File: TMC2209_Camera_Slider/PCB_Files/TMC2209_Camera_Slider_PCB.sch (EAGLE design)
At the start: 16 parts, among them J1 1X2-3.5MM

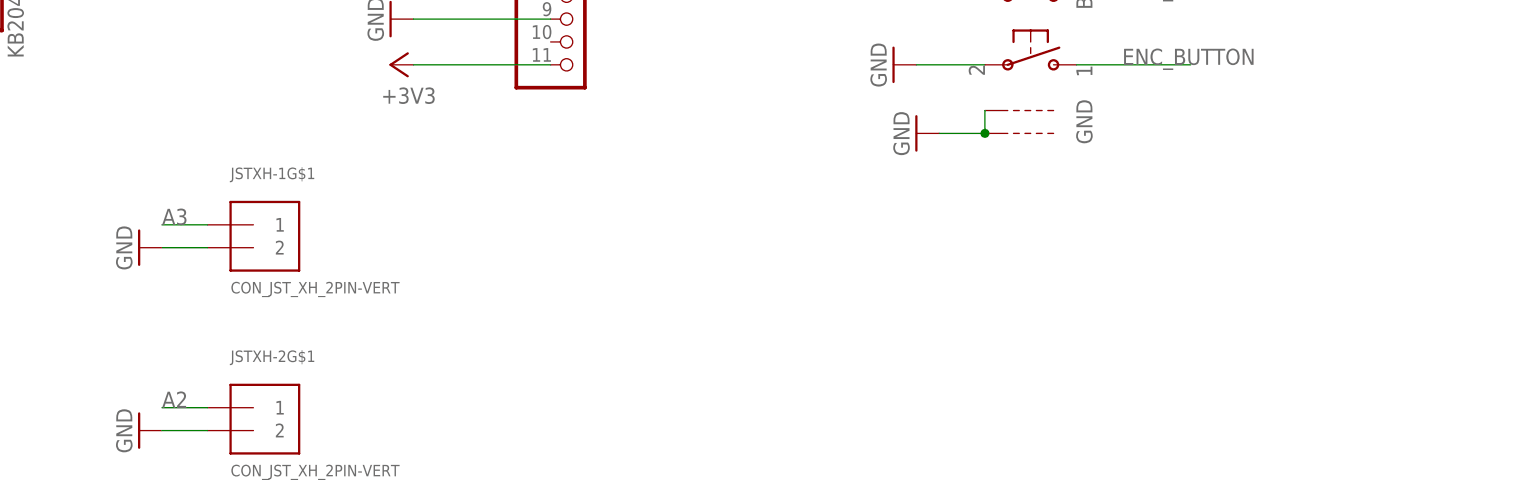
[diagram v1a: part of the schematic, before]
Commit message: switch jst xh connectors
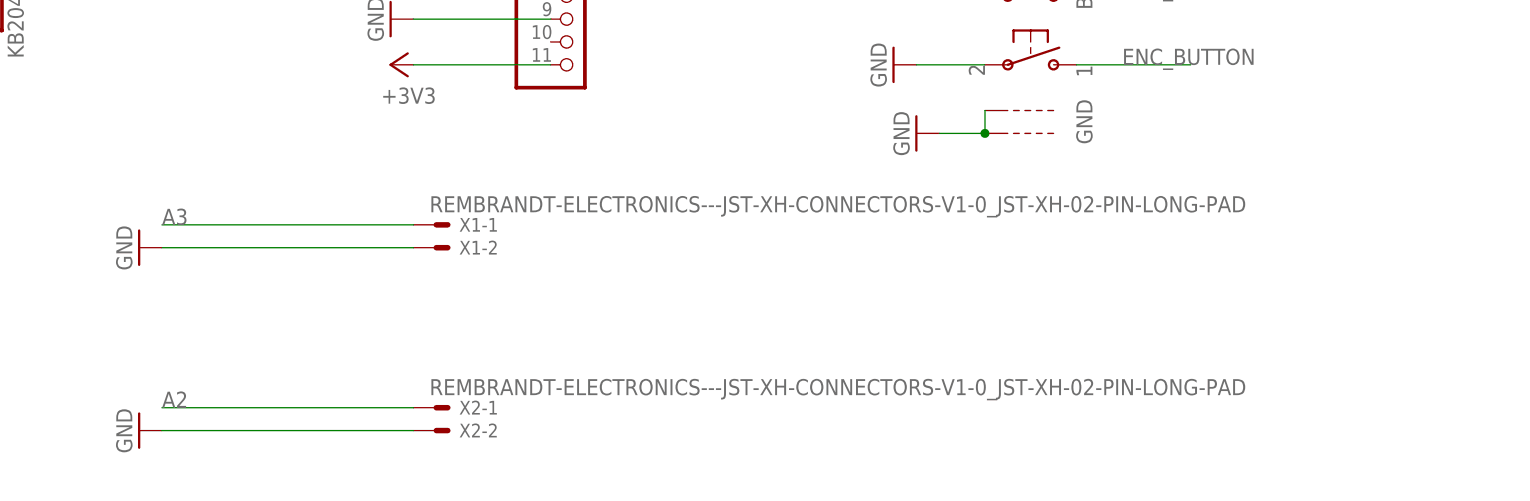
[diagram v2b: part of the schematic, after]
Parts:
- removed JSTXH-1, JSTXH-2: CON_JST_XH_2PIN-VERT, adafruit_electromech:CON_JST_XH_2PIN-VERT
- added X1, X2: REMBRANDT-ELECTRONICS---JST-XH-CONNECTORS-V1-0_JST-XH-02-PI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, thermalBonnet:REMBRANDT-ELECTRONICS---JST-XH-CONNECTORS-V1-0_JST-XH-02-PIN-LONG-PAD
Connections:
- net A2: now also X2-1.S; no longer JSTXH-2G$1.1
- net A3: now also X1-1.S; no longer JSTXH-1G$1.1
- net GND: now also X1-2.S, X2-2.S; no longer JSTXH-1G$1.2, JSTXH-2G$1.2
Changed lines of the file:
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@@
 <part name="MPM3601" library="microbuilder" deviceset="HEADER-1X4" device=""/>
 <part name="TFT" library="microbuilder" deviceset="HEADER-1X11" device=""/>
-<part name="JSTXH-2" library="adafruit_electromech" deviceset="CON_JST_XH_2PIN" device="-VERT"/>
-<part name="JSTXH-1" library="adafruit_electromech" deviceset="CON_JST_XH_2PIN" device="-VERT"/>
 <part name="ROTARY" library="adafruit_electromech" deviceset="ENCODER_PLUS_SWITCH" device="_PEC11" technology="_BOURNS"/>
 <part name="DCJACK" library="adafruit_electromech" deviceset="DCBARREL" device="PTH"/>
@@
 <part name="P+5" library="supply1" library_urn="urn:adsk.eagle:library:371" deviceset="VCC" device=""/>
 <part name="GND13" library="supply1" library_urn="urn:adsk.eagle:library:371" deviceset="GND" device=""/>
+<part name="X1" library="thermalBonnet" deviceset="REMBRANDT-ELECTRONICS---JST-XH-CONNECTORS-V1-0_JST-XH-02-PIN" device="-LONG-PAD"/>
+<part name="X2" library="thermalBonnet" deviceset="REMBRANDT-ELECTRONICS---JST-XH-CONNECTORS-V1-0_JST-XH-02-PIN" device="-LONG-PAD"/>
 </parts>
 <sheets>
@@
 <attribute name="VALUE" x="95.25" y="12.7" size="1.778" layer="96"/>
 </instance>
-<instance part="JSTXH-2" gate="G$1" x="66.04" y="-22.86" smashed="yes">
-<attribute name="VALUE" x="63.5" y="-27.94" size="1.27" layer="96"/>
-<attribute name="NAME" x="63.5" y="-15.24" size="1.27" layer="95"/>
-</instance>
-<instance part="JSTXH-1" gate="G$1" x="66.04" y="-2.54" smashed="yes">
-<attribute name="VALUE" x="63.5" y="-7.62" size="1.27" layer="96"/>
-<attribute name="NAME" x="63.5" y="5.08" size="1.27" layer="95"/>
-</instance>
 <instance part="ROTARY" gate="G$1" x="152.4" y="25.4" smashed="yes">
 <attribute name="VALUE" x="150.495" y="36.83" size="1.778" layer="96"/>
@@
 <instance part="GND13" gate="1" x="127" y="78.74" smashed="yes" rot="MR180">
 <attribute name="VALUE" x="124.46" y="81.28" size="1.778" layer="96" rot="MR180"/>
+</instance>
+<instance part="X1" gate="-1" x="86.36" y="0" smashed="yes">
+<attribute name="NAME" x="88.9" y="-0.762" size="1.524" layer="95"/>
+<attribute name="VALUE" x="85.598" y="1.397" size="1.778" layer="96"/>
+</instance>
+<instance part="X1" gate="-2" x="86.36" y="-2.54" smashed="yes">
+<attribute name="NAME" x="88.9" y="-3.302" size="1.524" layer="95"/>
+</instance>
+<instance part="X2" gate="-1" x="86.36" y="-20.32" smashed="yes">
+<attribute name="NAME" x="88.9" y="-21.082" size="1.524" layer="95"/>
+<attribute name="VALUE" x="85.598" y="-18.923" size="1.778" layer="96"/>
+</instance>
+<instance part="X2" gate="-2" x="86.36" y="-22.86" smashed="yes">
+<attribute name="NAME" x="88.9" y="-23.622" size="1.524" layer="95"/>
 </instance>
 </instances>
@@
 </segment>
 <segment>
-<pinref part="JSTXH-2" gate="G$1" pin="2"/>
 <pinref part="GND10" gate="1" pin="GND"/>
-<wire x1="60.96" y1="-22.86" x2="55.88" y2="-22.86" width="0.1524" layer="91"/>
-</segment>
-<segment>
-<pinref part="JSTXH-1" gate="G$1" pin="2"/>
+<pinref part="X2" gate="-2" pin="S"/>
+<wire x1="55.88" y1="-22.86" x2="83.82" y2="-22.86" width="0.1524" layer="91"/>
+</segment>
+<segment>
 <pinref part="GND9" gate="1" pin="GND"/>
-<wire x1="60.96" y1="-2.54" x2="55.88" y2="-2.54" width="0.1524" layer="91"/>
+<pinref part="X1" gate="-2" pin="S"/>
+<wire x1="55.88" y1="-2.54" x2="83.82" y2="-2.54" width="0.1524" layer="91"/>
 </segment>
 <segment>
@@
 </segment>
 <segment>
-<pinref part="JSTXH-1" gate="G$1" pin="1"/>
-<wire x1="60.96" y1="0" x2="55.88" y2="0" width="0.1524" layer="91"/>
 <label x="55.88" y="0" size="1.778" layer="95"/>
+<pinref part="X1" gate="-1" pin="S"/>
+<wire x1="55.88" y1="0" x2="83.82" y2="0" width="0.1524" layer="91"/>
 </segment>
 </net>
@@
 </segment>
 <segment>
-<pinref part="JSTXH-2" gate="G$1" pin="1"/>
-<wire x1="60.96" y1="-20.32" x2="55.88" y2="-20.32" width="0.1524" layer="91"/>
 <label x="55.88" y="-20.32" size="1.778" layer="95"/>
-</segment>
-</net>
+<pinref part="X2" gate="-1" pin="S"/>
+<wire x1="55.88" y1="-20.32" x2="83.82" y2="-20.32" width="0.1524" layer="91"/>
+</segment>
+</net>

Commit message: miso/mosi
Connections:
- removed net MI: KB2040-2.3, TFT.7
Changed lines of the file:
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@@
-</segment>
-</net>
-<net name="MI" class="0">
-<segment>
-<pinref part="KB2040-2" gate="G$1" pin="3"/>
-<wire x1="30.48" y1="50.8" x2="30.48" y2="60.96" width="0.1524" layer="91"/>
-<label x="30.48" y="58.42" size="1.778" layer="95" rot="R90"/>
-</segment>
-<segment>
-<pinref part="TFT" gate="G$1" pin="7"/>
-<wire x1="99.06" y1="27.94" x2="83.82" y2="27.94" width="0.1524" layer="91"/>
-<label x="83.82" y="27.94" size="1.778" layer="95"/>
 </segment>
 </net>
@@
 <net name="MO" class="0">
 <segment>
+<pinref part="TFT" gate="G$1" pin="6"/>
+<wire x1="99.06" y1="30.48" x2="83.82" y2="30.48" width="0.1524" layer="91"/>
+<label x="83.82" y="30.48" size="1.778" layer="95"/>
+</segment>
+<segment>
 <pinref part="KB2040-2" gate="G$1" pin="2"/>
 <wire x1="33.02" y1="50.8" x2="33.02" y2="60.96" width="0.1524" layer="91"/>
 <label x="33.02" y="55.88" size="1.778" layer="95" rot="R90"/>
 </segment>
-<segment>
-<pinref part="TFT" gate="G$1" pin="6"/>
-<wire x1="99.06" y1="30.48" x2="83.82" y2="30.48" width="0.1524" layer="91"/>
-<label x="83.82" y="30.48" size="1.778" layer="95"/>
-</segment>
 </net>
